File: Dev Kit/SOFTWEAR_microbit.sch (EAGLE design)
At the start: 27 parts, among them J1 455-1750-1-ND, J4 QWIIC_RIGHT_ANGLE, J6 QWIIC_RIGHT_ANGLE, M1 MOTORSMD, Q1 500mA/300V, U5 OPA344, U6 ADMP401, U7 APDS-9960, X1 SM03B-SRSS-TB, X2 SM03B-SRSS-TB, X4 SM03B-SRSS-TB

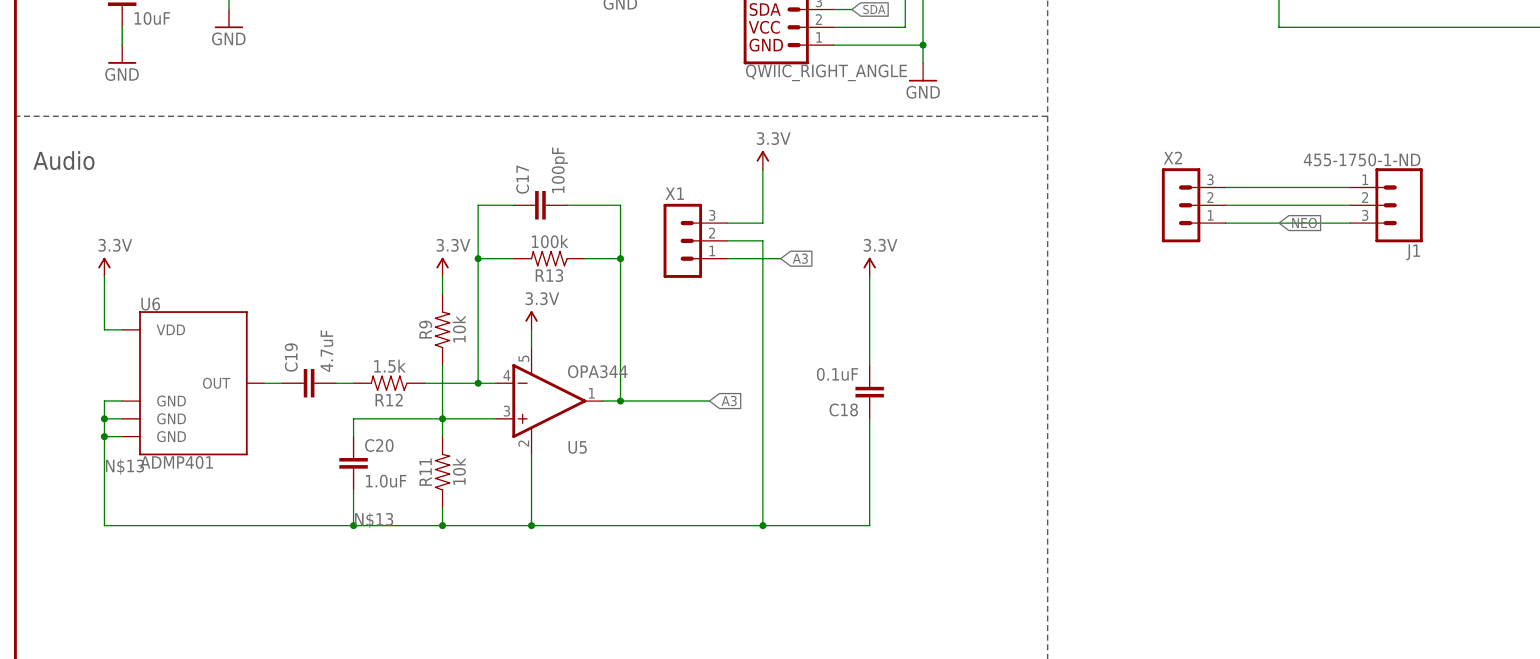
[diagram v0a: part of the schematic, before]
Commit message: added cap touch BOB
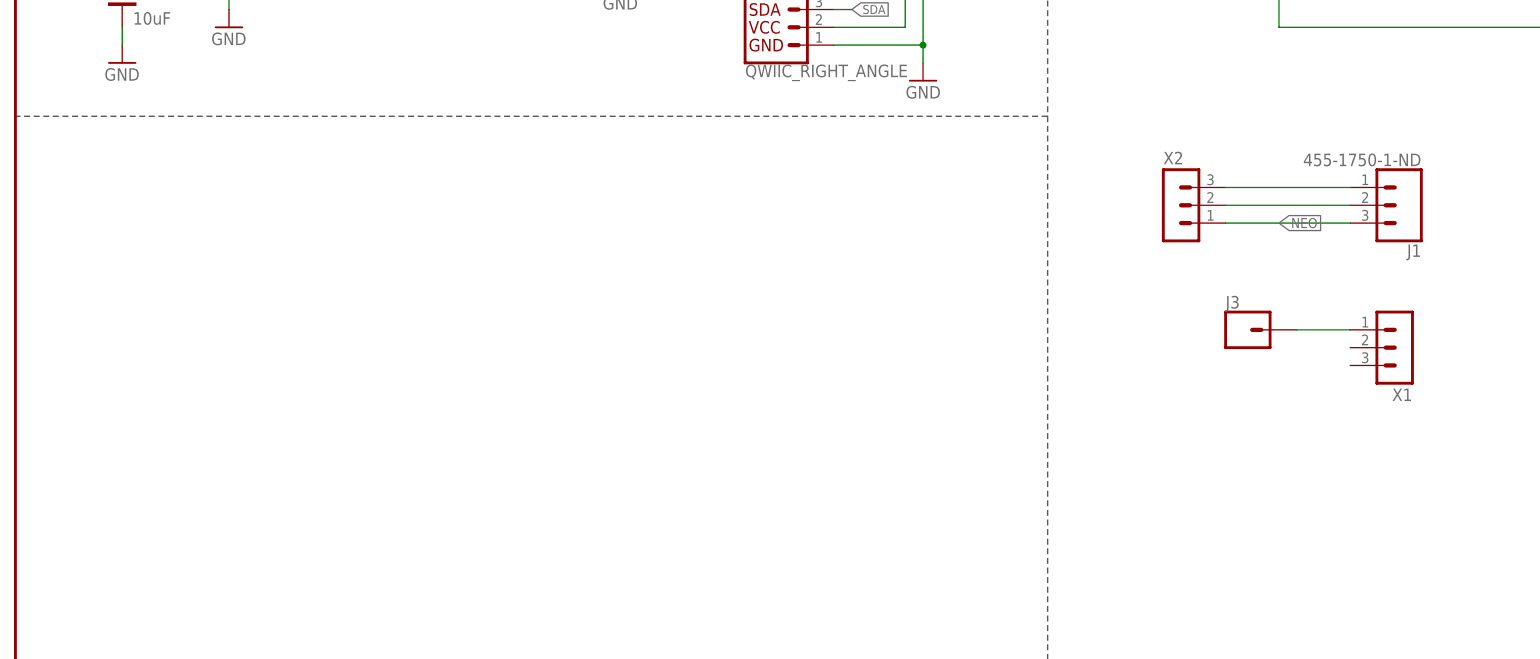
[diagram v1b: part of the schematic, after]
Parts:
- removed C17: 100pF, SparkFun-Capacitors:100PF-0603-50V-5%
- removed C18: 0.1uF, SparkFun-Capacitors:0.1UF-0603-25V-(+80/-20%)
- removed C19: 4.7uF, SparkFun-Capacitors:4.7UF-0603-6.3V-(10%)
- removed C20: 1.0uF, SparkFun-Capacitors:1.0UF-0603-16V-10%
- removed R11, R9: 10k, SparkFun-Resistors:10KOHM-0603-1/10W-1%
- removed R12: 1.5k, SparkFun-Resistors:1.5KOHM-0603-1/10W-1%
- removed R13: 100k, SparkFun-Resistors:100KOHM-0603-1/10W-1%
- removed U5: OPA344, SparkFun:OPA344
- removed U6: ADMP401, SparkFun-Sensors:ADMP401
- added J3: (no value), SparkFun-Connectors:CONN_01SPRING-CONN
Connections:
- removed net 3.3V: C18.2, R9.2, U5.V+, U6.VDD, X1.3
- removed net A3: C17.2, R13.1, U5.OUT, X1.1
- removed net N$1: C19.1, U6.OUT
- removed net N$10: C19.2, R12.2
- removed net N$11: C20.1, R11.2, R9.1, U5.+IN
- removed net N$13: C18.1, C20.2, R11.1, U5.V-, U6.GND@2, U6.GND@4, U6.GND@6, X1.2
- net N$6: now also J3.1, X1.1; no longer C17.1, R12.1, R13.2, U5.-IN
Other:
- note removed: "Audio"
- moved on the sheet: X1
